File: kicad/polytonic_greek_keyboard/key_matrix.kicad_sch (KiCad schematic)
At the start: 0 parts

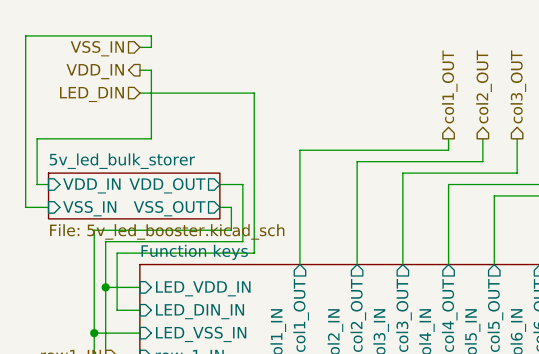
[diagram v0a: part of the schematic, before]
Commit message: [ADD] a more structured approach of the pcb in a way that won't overload the esp32 that is running it
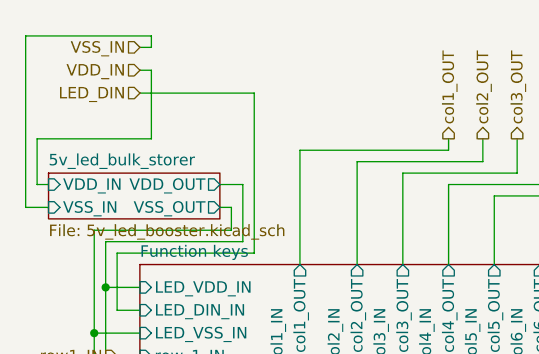
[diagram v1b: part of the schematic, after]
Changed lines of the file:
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@@
 	)
 	(hierarchical_label "VDD_IN"
-		(shape output)
+		(shape input)
 		(at 25.4 16.51 180)
 		(effects

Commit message: [UPDATE] the final merged version of the schematic before splitting into two separate kicad projects
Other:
- company: (none) -> Henry's Software House
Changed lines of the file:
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@@
 	(generator_version "9.0")
 	(paper "A4")
+	(title_block
+		(rev "1 - do not edit connector pin layout.")
+		(company "Henry's Software House")
+	)
 	(junction
 		(at 77.47 142.24)
